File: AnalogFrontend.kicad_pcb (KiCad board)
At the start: 2 copper layers, 1 part, among them U1 SE5004L

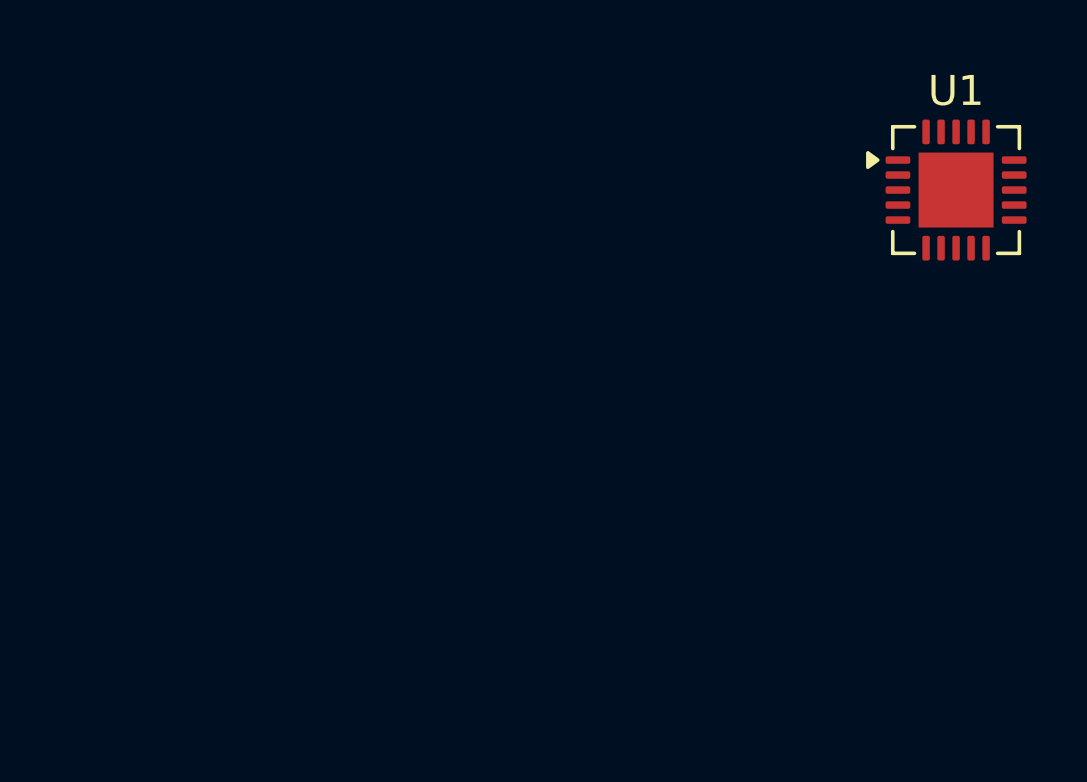
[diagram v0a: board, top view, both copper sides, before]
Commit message: update schematic
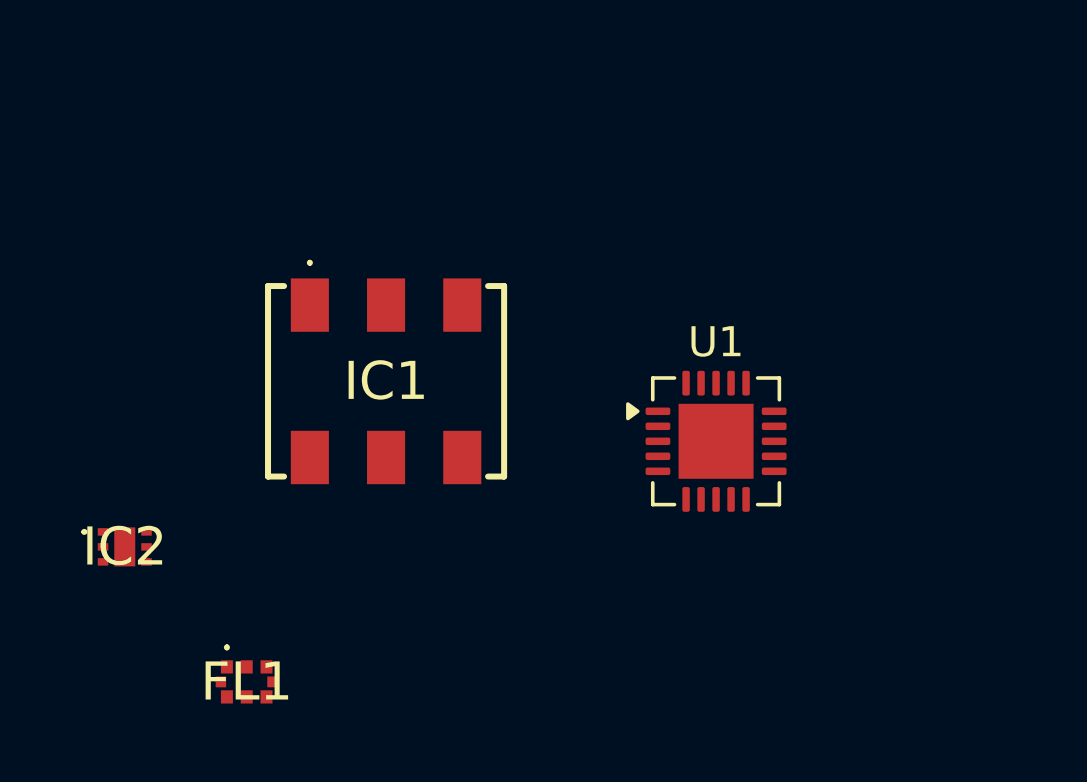
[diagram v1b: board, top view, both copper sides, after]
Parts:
- added FL1: LLP.2500.X.B.30, SamacSys_Parts:LLP2500XB30, F.Cu at (128.9, 115.0)
- added IC1: RMS-30+, SamacSys_Parts:RMS30, F.Cu at (133.5, 105.0)
- added IC2: SKY65405-21, SamacSys_Parts:SKY6540521, F.Cu at (124.8, 110.5)
- moved U1 11.6 mm to (144.5, 107.0)

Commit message: updatged schematics
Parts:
- added C10: 10pF, Capacitor_SMD:C_1206_3216Metric_Pad1.33x1.80mm_HandSolder, F.Cu at (155.5, 164.6)
- added C11: 0.1muF, Capacitor_SMD:C_1206_3216Metric_Pad1.33x1.80mm_HandSolder, F.Cu at (161.5, 144.5)
- added C12: 10pF, Capacitor_SMD:C_1206_3216Metric_Pad1.33x1.80mm_HandSolder, F.Cu at (161.5, 147.9)
- added C13: 2.7mu, Capacitor_SMD:C_1206_3216Metric_Pad1.33x1.80mm_HandSolder, F.Cu at (161.5, 151.2)
- added C14: 39n, Capacitor_SMD:C_1206_3216Metric_Pad1.33x1.80mm_HandSolder, F.Cu at (161.5, 154.6)
- added C15: 1.2mu, Capacitor_SMD:C_1206_3216Metric_Pad1.33x1.80mm_HandSolder, F.Cu at (161.5, 157.9)
- added C16: 1n, Capacitor_SMD:C_1206_3216Metric_Pad1.33x1.80mm_HandSolder, F.Cu at (161.5, 161.3)
- added C17: 1n, Capacitor_SMD:C_1206_3216Metric_Pad1.33x1.80mm_HandSolder, F.Cu at (161.5, 164.6)
- added C18: 1n, Capacitor_SMD:C_1206_3216Metric_Pad1.33x1.80mm_HandSolder, F.Cu at (167.5, 144.5)
- added C19: 1n, Capacitor_SMD:C_1206_3216Metric_Pad1.33x1.80mm_HandSolder, F.Cu at (167.5, 147.9)
- added C20: 10n, Capacitor_SMD:C_1206_3216Metric_Pad1.33x1.80mm_HandSolder, F.Cu at (167.5, 151.2)
- added C21: 4.7muF, Capacitor_SMD:C_1206_3216Metric_Pad1.33x1.80mm_HandSolder, F.Cu at (167.5, 154.6)
- added C22: 4.7muF, Capacitor_SMD:C_1206_3216Metric_Pad1.33x1.80mm_HandSolder, F.Cu at (167.5, 157.9)
- added C23: 4.7muF, Capacitor_SMD:C_1206_3216Metric_Pad1.33x1.80mm_HandSolder, F.Cu at (134.0, 137.0)
- added C4: 4.7muF, Capacitor_SMD:C_1206_3216Metric_Pad1.33x1.80mm_HandSolder, F.Cu at (155.5, 144.5)
- added C5: 4.7muF, Capacitor_SMD:C_1206_3216Metric_Pad1.33x1.80mm_HandSolder, F.Cu at (155.5, 147.9)
- added C6: 4.7muF, Capacitor_SMD:C_1206_3216Metric_Pad1.33x1.80mm_HandSolder, F.Cu at (155.5, 151.2)
- added C7: 10pF, Capacitor_SMD:C_1206_3216Metric_Pad1.33x1.80mm_HandSolder, F.Cu at (155.5, 154.6)
- added C8: 0.1muF, Capacitor_SMD:C_1206_3216Metric_Pad1.33x1.80mm_HandSolder, F.Cu at (155.5, 157.9)
- added C9: 0.1muF, Capacitor_SMD:C_1206_3216Metric_Pad1.33x1.80mm_HandSolder, F.Cu at (155.5, 161.3)
- added IC4: SE2576L-R, SamacSys_Parts:QFN50P300X300X90-17N-D, F.Cu at (117.0, 117.0)
- added IC5: MAX2752EUA+, SamacSys_Parts:SOP65P490X110-8N, F.Cu at (114.7, 99.8)
- added IC6: RMS-30+, SamacSys_Parts:RMS30, F.Cu at (105.5, 102.5)
- added IC7: MAX2752EUA+, SamacSys_Parts:SOP65P490X110-8N, F.Cu at (114.7, 104.5)
- added J3: USB_A, Connector_USB:USB3_A_Molex_48393-001, F.Cu at (157.0, 130.0)
- added J6: USB_A, Connector_USB:USB3_A_Molex_48393-001, F.Cu at (173.1, 130.0)
- added J8: Conn_01x03_Pin, Connector_PinHeader_1.00mm:PinHeader_1x03_P1.00mm_Vertical_SMD_Pin1Left, F.Cu at (173.3, 145.4)
- added R1: R, Resistor_SMD:R_0612_1632Metric_Pad1.18x3.40mm_HandSolder, F.Cu at (100.2, 130.0)
- added R10: 680, Resistor_SMD:R_0612_1632Metric_Pad1.18x3.40mm_HandSolder, F.Cu at (117.8, 134.9)
- added R11: 51, Resistor_SMD:R_0612_1632Metric_Pad1.18x3.40mm_HandSolder, F.Cu at (100.2, 139.9)
- added R12: 499, Resistor_SMD:R_0612_1632Metric_Pad1.18x3.40mm_HandSolder, F.Cu at (104.6, 139.9)
- added R13: 33.2k, Resistor_SMD:R_0612_1632Metric_Pad1.18x3.40mm_HandSolder, F.Cu at (109.0, 139.9)
- added R14: 200k, Resistor_SMD:R_0612_1632Metric_Pad1.18x3.40mm_HandSolder, F.Cu at (113.4, 139.9)
- added R15: 453k, Resistor_SMD:R_0612_1632Metric_Pad1.18x3.40mm_HandSolder, F.Cu at (134.7, 130.0)
- added R16: 49.9k, Resistor_SMD:R_0612_1632Metric_Pad1.18x3.40mm_HandSolder, F.Cu at (129.7, 120.0)
- added R2: R, Resistor_SMD:R_0612_1632Metric_Pad1.18x3.40mm_HandSolder, F.Cu at (104.6, 130.0)
- added R3: 200k, Resistor_SMD:R_0612_1632Metric_Pad1.18x3.40mm_HandSolder, F.Cu at (109.0, 130.0)
- added R4: 33.2k, Resistor_SMD:R_0612_1632Metric_Pad1.18x3.40mm_HandSolder, F.Cu at (113.4, 130.0)
- added R5: 499, Resistor_SMD:R_0612_1632Metric_Pad1.18x3.40mm_HandSolder, F.Cu at (117.8, 130.0)
- added R6: 453k, Resistor_SMD:R_0612_1632Metric_Pad1.18x3.40mm_HandSolder, F.Cu at (100.2, 134.9)
- added R7: 49.9k, Resistor_SMD:R_0612_1632Metric_Pad1.18x3.40mm_HandSolder, F.Cu at (104.6, 134.9)
- added R8: 4.7k, Resistor_SMD:R_0612_1632Metric_Pad1.18x3.40mm_HandSolder, F.Cu at (109.0, 134.9)
- added R9: 360, Resistor_SMD:R_0612_1632Metric_Pad1.18x3.40mm_HandSolder, F.Cu at (113.4, 134.9)
- added U2: LT3042xMSE, Package_SO:MSOP-10-1EP_3x3mm_P0.5mm_EP1.68x1.88mm, F.Cu at (159.7, 93.3)
- added U3: LT3042xMSE, Package_SO:MSOP-10-1EP_3x3mm_P0.5mm_EP1.68x1.88mm, F.Cu at (161.6, 103.0)
- added Y1: ATX-H11-F-25.000MHz-F25-T, SamacSys_Parts:ATXH11F25000MHzF25T, F.Cu at (172.1, 95.2)
- U1: value SE5004L -> ADF4351; footprint Package_DFN_QFN:QFN-20-1EP_4x4mm_P0.5mm_EP2.5x2.5mm -> Package_CSP:LFCSP-32-1EP_5x5mm_P0.5mm_EP3.25x3.25mm
- moved FL1 19.4 mm to (109.5, 115.5)
- moved U1 11.1 mm to (142.9, 118.0)
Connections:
- FL1 pad 1: unconnected-(FL1-Pad1) -> GND
- FL1 pad 2: unconnected-(FL1-Pad2) -> GND
- FL1 pad 3: unconnected-(FL1-Pad3) -> GND
- FL1 pad 4: Net-(IC1-IF) -> Net-(IC1-RF)
- FL1 pad 5: Net-(IC2-RF_IN) -> Net-(IC4-RF_IN)
- FL1 pad 6: unconnected-(FL1-Pad6) -> GND
- FL1 pad 7: unconnected-(FL1-Pad7) -> GND
- FL1 pad 8: unconnected-(FL1-Pad8) -> GND
- IC1 pad 1: unconnected-(IC1-LO-Pad1) -> /Oscillator TX Output
- IC2 pad 1: unconnected-(IC2-V_ENABLE_-Pad1) -> +5V
- IC2 pad 6: /5.0V -> +5V
- U1 pad 1: GND -> Net-(J8-Pin_1)
- U1 pad 10: unconnected-(U1-DET-Pad10) -> +3.3V
- U1 pad 12: GND -> Net-(U1-RF_OUT_A+)
- U1 pad 13: unconnected-(U1-RFOUT-Pad13) -> Net-(U1-RF_OUT_A-)
- U1 pad 14: GND -> unconnected-(U1-RF_OUT_B+-Pad14)
- U1 pad 15: GND -> unconnected-(U1-RF_OUT_B--Pad15)
- U1 pad 16: GND -> unconnected-(U1-VVCO-Pad16)
- U1 pad 17: GND -> unconnected-(U1-VVCO-Pad17)
- U1 pad 18: unconnected-(U1-VCC3-Pad18) -> GND
- U1 pad 19: unconnected-(U1-VCC2-Pad19) -> Net-(U1-TEMP)
- U1 pad 2: GND -> Net-(J8-Pin_2)
- U1 pad 20: unconnected-(U1-VCC1-Pad20) -> Net-(U1-VTUNE)
- U1 pad 3: unconnected-(U1-RFIN-Pad3) -> Net-(J8-Pin_3)
- U1 pad 4: GND -> +3.3V
- U1 pad 6: unconnected-(U1-SP1-Pad6) -> +3.3V
- U1 pad 7: unconnected-(U1-SP2-Pad7) -> Net-(U1-CPout)
- U1 pad 8: unconnected-(U1-VCC2-Pad8) -> GND
- U1 pad 9: unconnected-(U1-VCC3-Pad9) -> GND

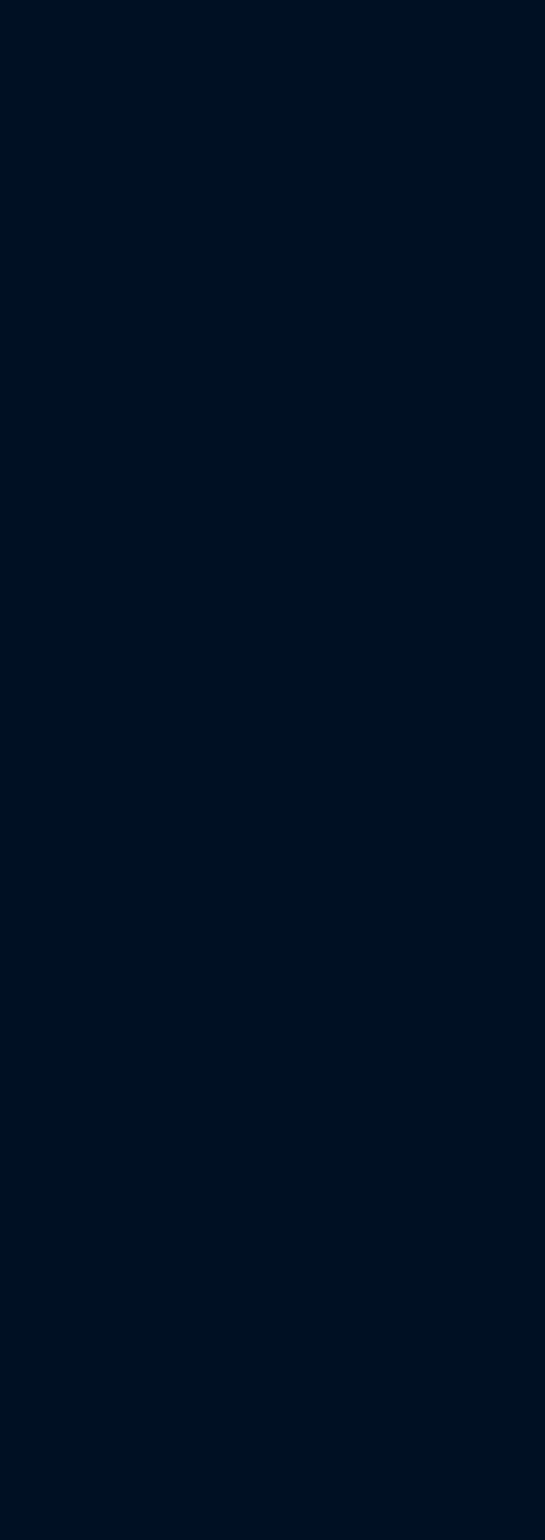
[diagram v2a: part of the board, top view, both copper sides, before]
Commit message: updated schematics
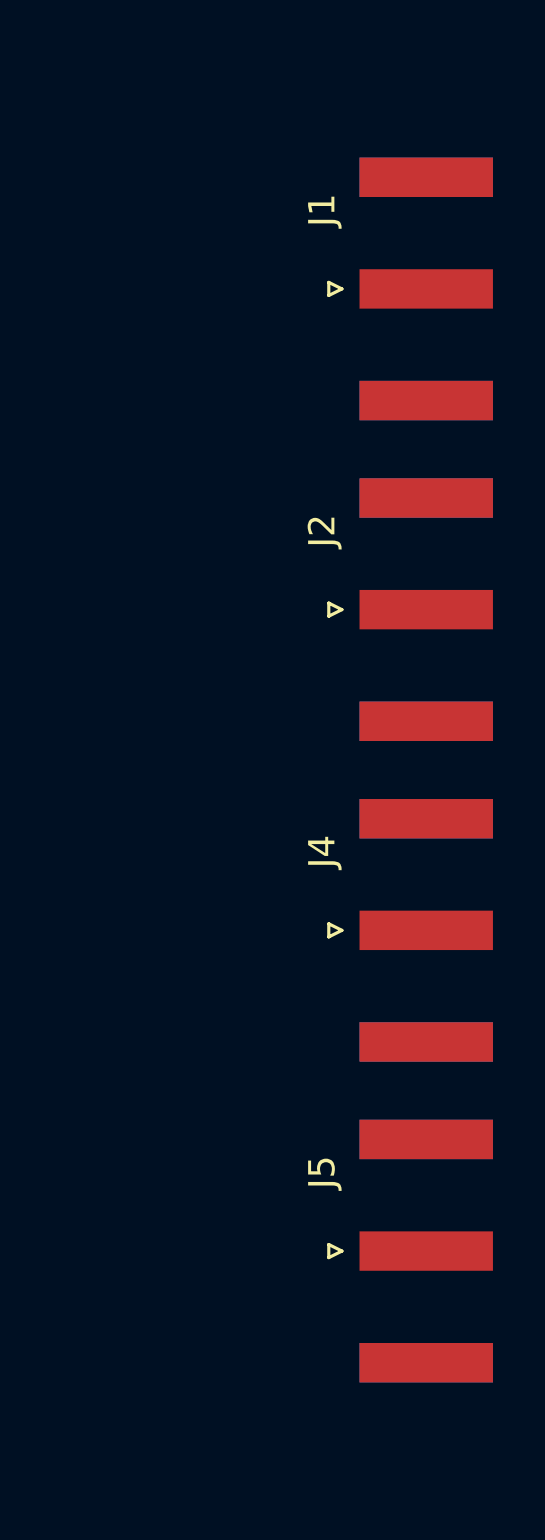
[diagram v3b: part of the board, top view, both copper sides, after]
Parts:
- added J1: Conn_Coaxial_x2, Connector_Coaxial:SMA_Amphenol_132289_EdgeMount, F.Cu at (204.8, 102.1)
- added J2: Conn_Coaxial_x2, Connector_Coaxial:SMA_Amphenol_132289_EdgeMount, F.Cu at (204.8, 114.3)
- added J4: Conn_Coaxial_x2, Connector_Coaxial:SMA_Amphenol_132289_EdgeMount, F.Cu at (204.8, 126.5)
- added J5: Conn_Coaxial_x2, Connector_Coaxial:SMA_Amphenol_132289_EdgeMount, F.Cu at (204.8, 138.7)
